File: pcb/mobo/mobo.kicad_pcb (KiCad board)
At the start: 2 copper layers, 51.6 x 89 mm, 78 parts, among them J1 SWD_10, J2 PEEL_MOTOR, J3 DRIVE_MOTOR, J5 SPRING_FINGERS, J8 USART1, J9 SWD_10, U1 STM32F031C6Tx, U2 STM32F031K6Ux, U4 AP1117-33, U5 MC34063AD, U6 MAX3078E, U7 DRV8837, U8 DRV8837, Y1 8MHz

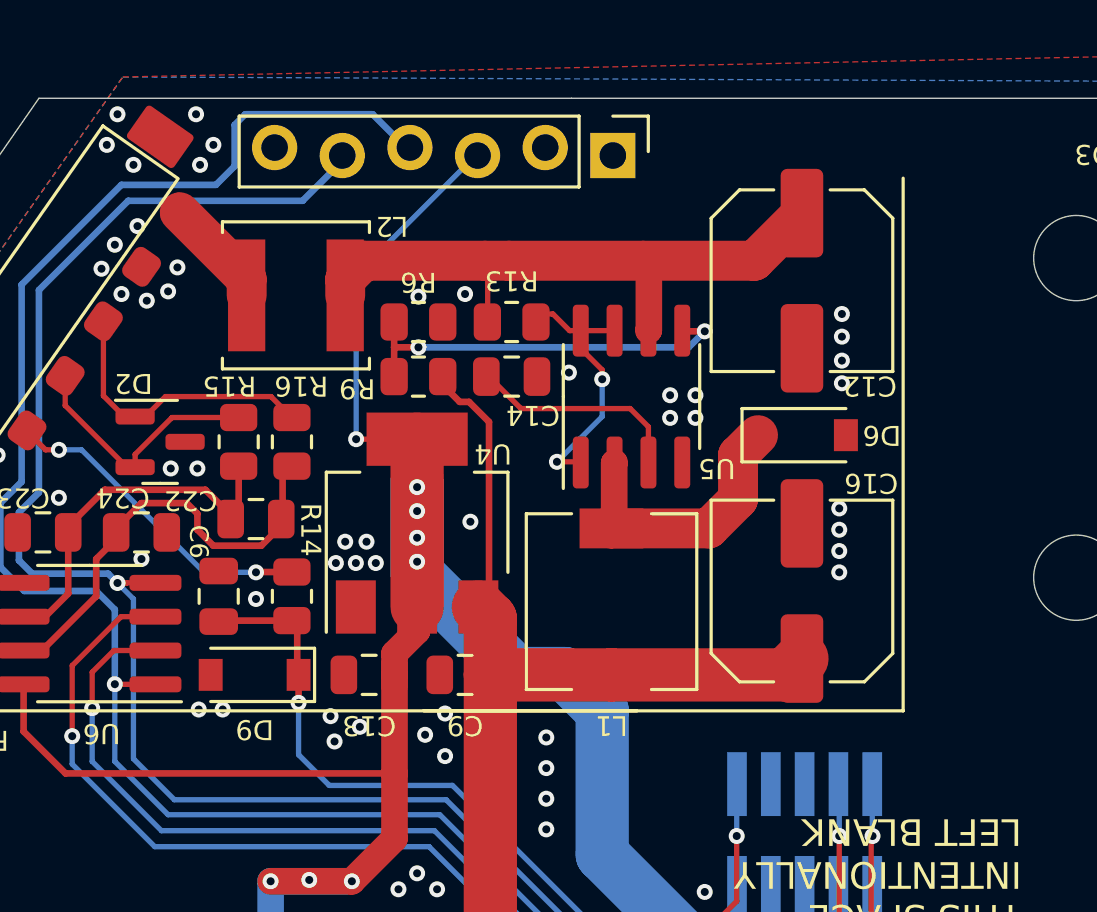
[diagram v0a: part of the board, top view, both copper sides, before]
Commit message: updated to 8mm filter cap footprint
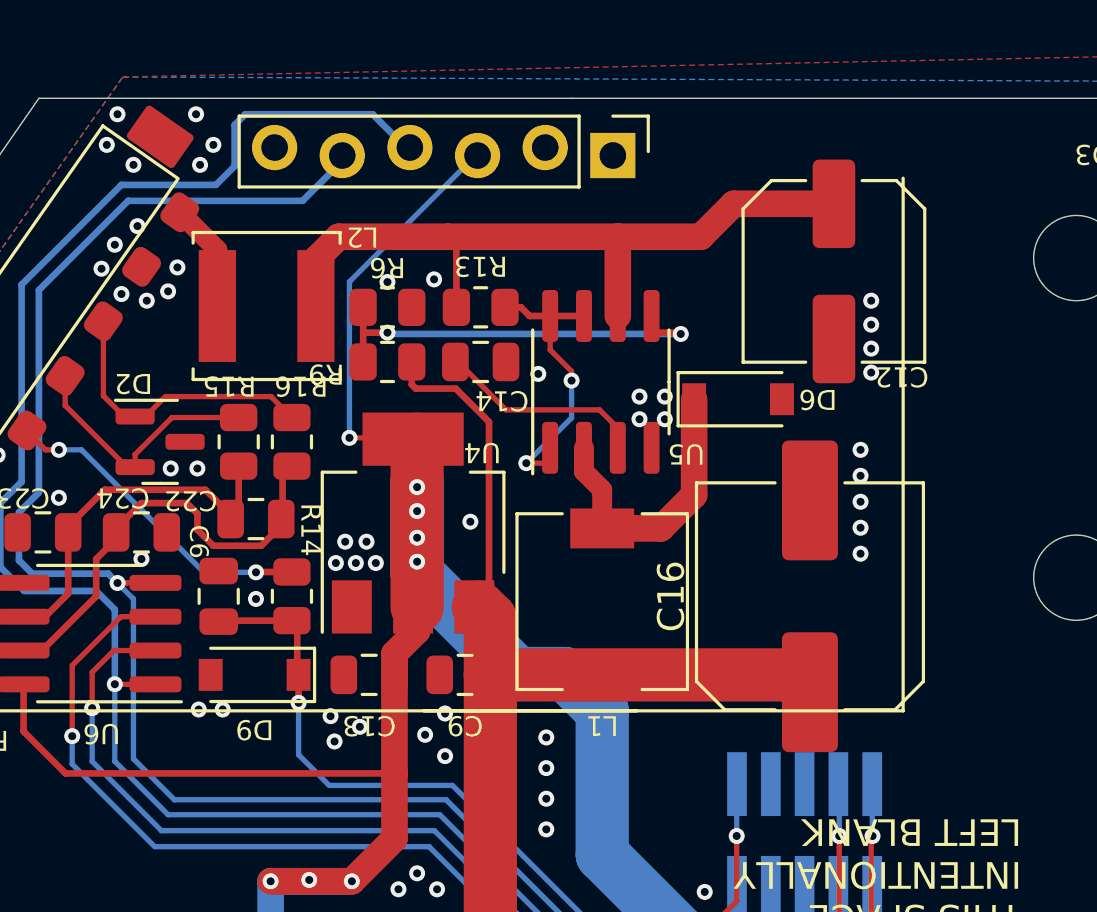
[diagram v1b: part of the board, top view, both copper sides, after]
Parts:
- C16: footprint Capacitor_SMD:C_Elec_6.3x7.7 -> Capacitor_SMD:C_Elec_8x10.2
- moved D6 2.75 mm to (133.1, 41.1)
- moved R13 1.29 mm to (123.4, 37.6)
- moved R6 1.29 mm to (119.9, 37.6)
- moved C14 1.29 mm to (123.4, 39.7)
- moved R9 1.29 mm to (119.9, 39.7)
- moved U5 1.27 mm to (128.0, 40.5)
- moved C12 1.25 mm to (136.7, 36.3)
- moved L2 1.17 mm to (115.4, 37.6)
- moved C16 0.36 mm to (135.8, 48.5)
- moved L1 0.35 mm to (128.0, 48.7)
- moved U4 0.15 mm to (120.9, 45.8)
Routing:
- net +VDC: track 23.6 -> 27.9 mm
- net +10V: track 81.6 -> 83.6 mm
- net GND: vias 114 -> 115
